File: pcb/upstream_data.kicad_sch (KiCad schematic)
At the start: 11 parts, among them J1 USB-C, U1 USBLC6-2SC6

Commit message: every bill-of-materials line answers the assembler
The first upload to the fabricator matched the passives by value and package and failed nine
lines. Each line now carries a definite answer in the schematic, written out as columns: a
catalogue number where the part is in the catalogue -- the flash, the protection arrays, the
indicators, the ferrite, and both crystals as 10 pF parts, since the catalogue's basic crystals
are 20 pF and the processor vendor's circuit was copied with its 15 pF capacitors; a named part
and a global-sourcing note where it is not -- the buck inductor, the buttons, the USB-C receptacle
and the USB-A sockets. The debug header is marked not fitted, and the mounting holes leave the
bill and the placement file, since neither is a part.

The same fields are on the board's footprints, as an update from the schematic would put them, so
parity holds; the export writes the sourcing column; the design document carries the table.

Co-Authored-By: Claude Fable 5.1 <noreply@anthropic.com>
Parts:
- J1: MPN (none) -> GCT USB4105-GF-A; Sourcing (none) -> JLCPCB global sourcing
- U1: LCSC (none) -> C7519; MPN (none) -> USBLC6-2SC6
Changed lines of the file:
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@@
+			)
+		)
+		(property "Sourcing" "JLCPCB global sourcing"
+			(at 76.2 93.98 0)
+			(show_name no)
+			(do_not_autoplace no)
+			(hide yes)
+			(effects
+				(font
+					(size 1.27 1.27)
+				)
+			)
+		)
+		(property "MPN" "GCT USB4105-GF-A"
+			(at 76.2 93.98 0)
+			(show_name no)
+			(do_not_autoplace no)
+			(hide yes)
+			(effects
+				(font
+					(size 1.27 1.27)
+				)
 			)
 		)
@@
 			(effects
 				(font
+					(size 1.27 1.27)
+				)
+				(justify left)
+			)
+		)
+		(property "LCSC" "C7519"
+			(at 142.6211 106.68 0)
+			(show_name no)
+			(do_not_autoplace no)
+			(hide yes)
+			(effects
+				(font
+					(size 1.27 1.27)
+				)
+				(justify left)
+			)
+		)
+		(property "MPN" "USBLC6-2SC6"
+			(at 142.6211 106.68 0)
+			(show_name no)
+			(do_not_autoplace no)
+			(hide yes)
+			(effects
+				(font

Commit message: the four sourced lines become catalogue parts
Global sourcing turned out to be a pre-purchase into one's own library, three to four weeks and an
inspection fee per kind of connector or switch, so the connectors, the buttons and the prototype's
inductor come from the catalogue instead, each checked against a drawing rather than a part page:

- USB-C: Korean Hroparts TYPE-C-31-M-12 (C165948). KiCad's footprint for it has the GCT part's
  pegs and shell slots with the pad row 0.38 mm further out; the footprint is swapped on the board
  with the pads kept on the old row and the body moved toward the edge, as a project copy with its
  silkscreen stopped inside the edge, like the sockets'. GCT's own USB4215 is not a drop-in.
- USB-A: TE 292303-6 (C591765), through-hole right angle on the Molex pattern.
- buttons: C&K KSC221JLFS (C221726), the same 6.2 mm J-lead family as the KSC6 drawn.
- buck inductor: Sunlord SWPA4030S4R7MT (C57269) for the prototype; the Coilcraft stays the
  production part.

Parity holds. Four clearances of 0.01 to 0.14 mm remain in the receptacle's hand-routed breakout,
where the longer pads now reach it; they are the next edit, and the export waits on them.

Co-Authored-By: Claude Fable 5.1 <noreply@anthropic.com>
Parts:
- J1: footprint Connector_USB:USB_C_Receptacle_GCT_USB4105-xx-A_16P_TopMnt_Horizontal -> crossfire:USB_C_Receptacle_HRO_TYPE-C-31-M-12_Overhang; LCSC (none) -> C165948; MPN GCT USB4105-GF-A -> Korean Hroparts TYPE-C-31-M-12; Sourcing JLCPCB global sourcing -> (none)
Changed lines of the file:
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@@
 			)
 		)
-		(property "Sourcing" "JLCPCB global sourcing"
+		(property "LCSC" "C165948"
 			(at 76.2 93.98 0)
 			(show_name no)
@@
 			)
 		)
-		(property "MPN" "GCT USB4105-GF-A"
+		(property "Sourcing" ""
 			(at 76.2 93.98 0)
 			(show_name no)
@@
 			)
 		)
-		(property "Footprint" "Connector_USB:USB_C_Receptacle_GCT_USB4105-xx-A_16P_TopMnt_Horizontal"
+		(property "MPN" "Korean Hroparts TYPE-C-31-M-12"
+			(at 76.2 93.98 0)
+			(show_name no)
+			(do_not_autoplace no)
+			(hide yes)
+			(effects
+				(font
+					(size 1.27 1.27)
+				)
+			)
+		)
+		(property "Footprint" "crossfire:USB_C_Receptacle_HRO_TYPE-C-31-M-12_Overhang"
 			(at 76.2 114.3 0)
 			(hide yes)

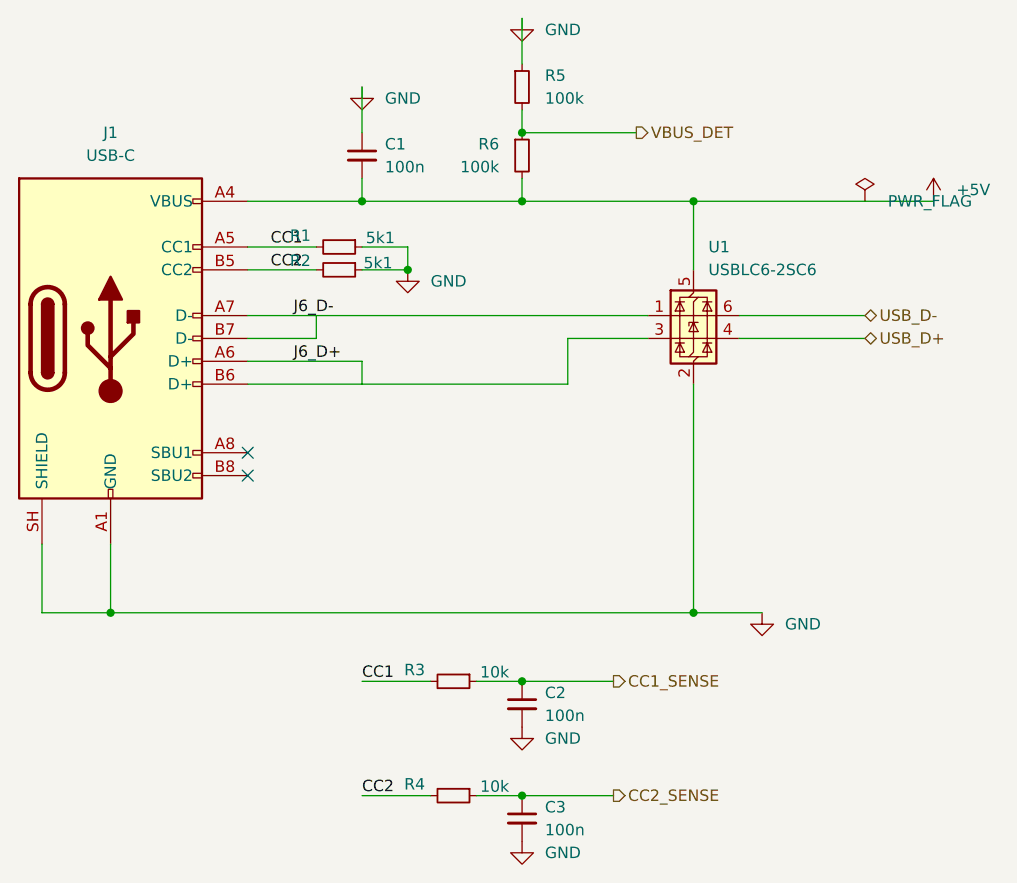
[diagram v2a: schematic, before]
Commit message: a resettable fuse on the 5 V input
F1, a 1812 polymer fuse with a 2.6 A hold and a 5 A trip, goes in series with VBUS at the
receptacle, ahead of everything. The wire between the receptacle's four VBUS pins and the fuse is
its own net, VBUS_IN, in the heavy-copper class; everything after the fuse is +5V as before. On the
board the fuse sits 5 mm from the receptacle in a spot checked clear of every other net's copper,
with its pads on the two nets and the receptacle's VBUS pads moved to the new one. The copper from
those pads through the fuse to the 5 V vias is the next hand edit; until it is drawn the rules
check lists the old VBUS tracks as shorting the two nets. The design document says why a
resettable part and what it costs.

Co-Authored-By: Claude Fable 5.1 <noreply@anthropic.com>
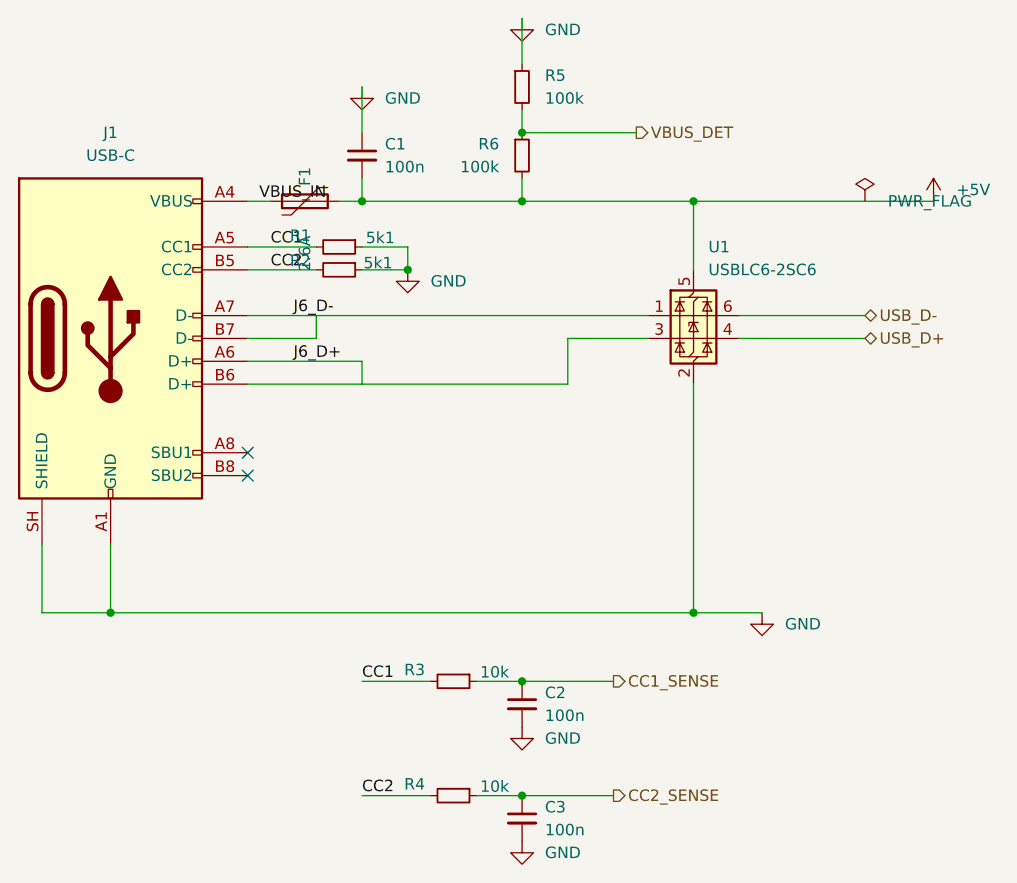
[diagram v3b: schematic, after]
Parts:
- added F1: 2.6A, Fuse:Fuse_1812_4532Metric, symbol Device:Polyfuse
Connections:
- net +5V: now also F1.2; no longer J1.A4 (VBUS), J1.A9 (VBUS), J1.B4 (VBUS), J1.B9 (VBUS)
- new net VBUS_IN: F1.1, J1.A4 (VBUS), J1.A9 (VBUS), J1.B4 (VBUS), J1.B9 (VBUS)
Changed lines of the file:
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@@
-	(wire
-		(pts
-			(xy 91.44 99.06) (xy 160.02 99.06)
-		)
-		(stroke
-			(width 0)
-			(type solid)
-		)
-	)
 	(wire
 		(pts
@@
 					(unit 1)
 				)
+			)
+		)
+	)
+	(wire
+		(pts
+			(xy 91.44 99.06) (xy 93.98 99.06)
+		)
+		(stroke
+			(width 0)
+			(type default)
+		)
+	)
+	(wire
+		(pts
+			(xy 101.6 99.06) (xy 160.02 99.06)
+		)
+		(stroke
+			(width 0)
+			(type default)
+		)
+	)
+	(label "VBUS_IN"
+		(at 92.71 99.06 0)
+		(effects
+			(font
+				(size 1.27 1.27)
+			)
+			(justify left bottom)
+		)
+	)
+	(symbol
+		(lib_id "Device:Polyfuse")
+		(at 97.79 99.06 90)
+		(unit 1)
+		(body_style 1)
+		(exclude_from_sim no)
+		(in_bom yes)
+		(on_board yes)
+		(in_pos_files yes)
+		(dnp no)
+		(fields_autoplaced yes)
+		(property "Reference" "F1"
+			(at 97.79 95.25 0)
+			(show_name no)
+			(do_not_autoplace no)
+			(effects
+				(font
+					(size 1.27 1.27)
+				)
+				(justify right)
+			)
+		)
+		(property "Value" "2.6A"
+			(at 97.79 102.87 0)
+			(show_name no)
+			(do_not_autoplace no)
+			(effects
+				(font
+					(size 1.27 1.27)
+				)
+				(justify right)
+			)
+		)
+		(property "Voltage" "8V"
+			(at 95.25 100.3299 0)
+			(show_name no)
+			(do_not_autoplace no)
+			(hide yes)
+			(effects
+				(font
+					(size 1.27 1.27)
+				)
+				(justify right)
+			)
+		)
+		(property "Trip" "5A"
+			(at 95.25 100.3299 0)
+			(show_name no)
+			(do_not_autoplace no)
+			(hide yes)
+			(effects
+				(font
+					(size 1.27 1.27)
+				)
+				(justify right)
+			)
+		)
+		(property "Hold" "2.6A"
+			(at 95.25 100.3299 0)
+			(show_name no)
+			(do_not_autoplace no)
+			(hide yes)
+			(effects
+				(font
+					(size 1.27 1.27)
+				)
+				(justify right)
+			)
+		)
+		(property "LCSC" "C70127"
+			(at 95.25 100.3299 0)
+			(show_name no)
+			(do_not_autoplace no)
+			(hide yes)
+			(effects
+				(font
+					(size 1.27 1.27)
+				)
+				(justify right)
+			)
+		)
+		(property "MPN" "TECHFUSE mSMD260"
+			(at 95.25 100.3299 0)
+			(show_name no)
+			(do_not_autoplace no)
+			(hide yes)
+			(effects
+				(font
+					(size 1.27 1.27)
+				)
+				(justify right)
+			)
+		)
+		(property "Footprint" "Fuse:Fuse_1812_4532Metric"
+			(at 97.79 99.06 0)
+			(hide yes)
+			(show_name no)
+			(do_not_autoplace no)
+			(effects
+				(font
+					(size 1.27 1.27)
+				)
+			)
+		)
+		(property "Datasheet" ""
+			(at 97.79 99.06 0)
+			(hide yes)
+			(show_name no)
+			(do_not_autoplace no)
+			(effects
+				(font
+					(size 1.27 1.27)
+				)
+			)
+		)
+		(property "Description" "resettable fuse, 2.6 A hold, 5 A trip, 8 V, 1812"
+			(at 97.79 99.06 0)
+			(hide yes)
+			(show_name no)
+			(do_not_autoplace no)
+			(effects
+				(font
+					(size 1.27 1.27)
+				)
+			)
+		)
+		(pin "1"
+		)
+		(pin "2"
+		)
+		(instances
+			(project "crossfire"
+				(path "/4c5cdd13-4f54-43b0-affb-0ae4b9a4d279/9de577d2-4349-45dc-ab43-167b038179a9"
+					(reference "F1")
+					(unit 1)
+				)
